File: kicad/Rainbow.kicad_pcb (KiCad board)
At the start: 2 copper layers, 14 parts, among them J1 PICKit3, J2 UART, J3 POWER, J5 RGB, J6 RGB, J7 RGB, J8 RGB, Q1 2N7000, Q2 2N7000, Q3 2N7000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

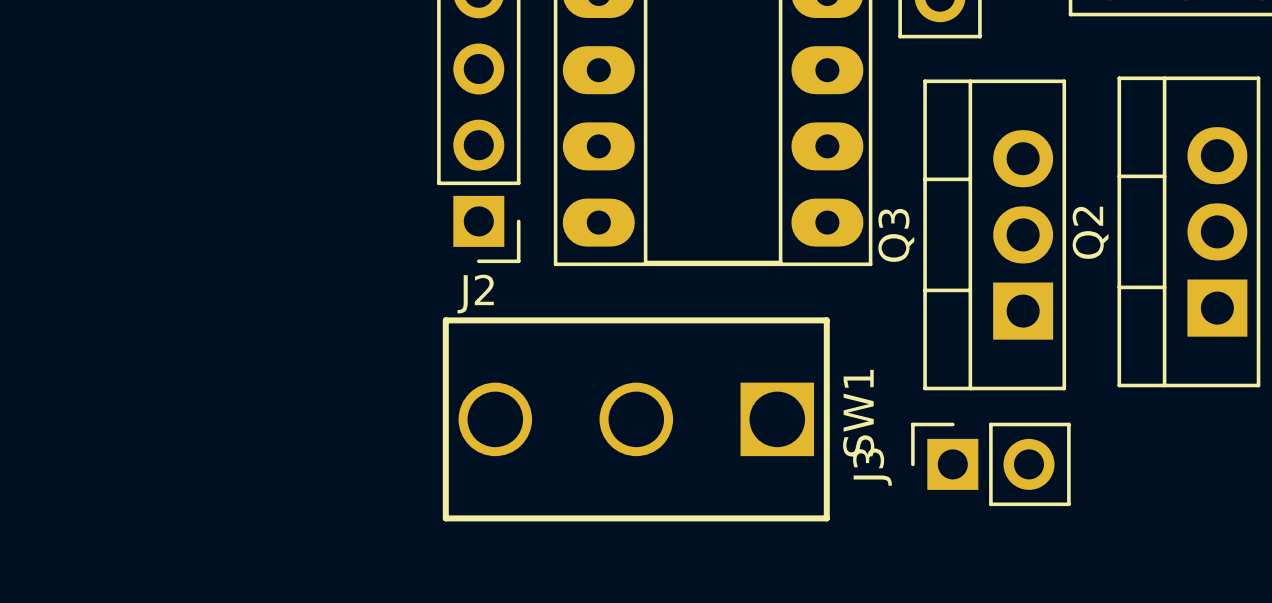
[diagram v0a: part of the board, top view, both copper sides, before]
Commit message: Add capacitors to power supply
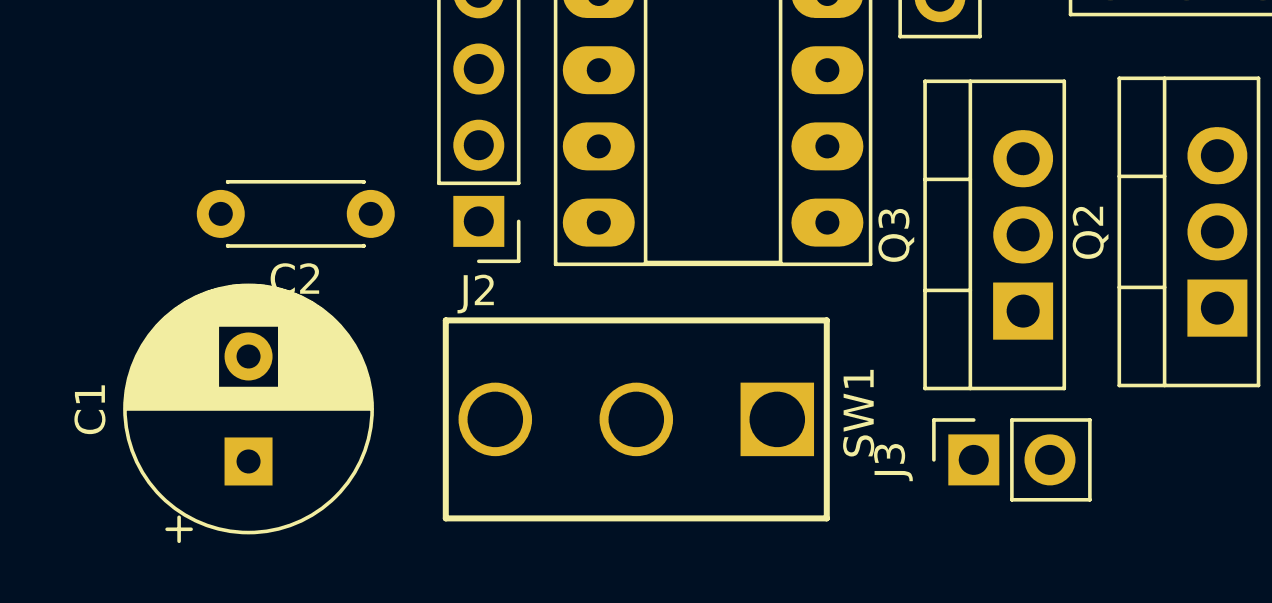
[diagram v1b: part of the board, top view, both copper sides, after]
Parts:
- added C1: 470uF, Capacitor_THT:CP_Radial_D8.0mm_P3.50mm, F.Cu at (107.2, 100.8)
- added C2: 0.1uF, Capacitor_THT:C_Disc_D4.3mm_W1.9mm_P5.00mm, F.Cu at (111.3, 92.5)
- moved J3 0.72 mm to (131.4, 100.7)

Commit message: A bunch of stuff
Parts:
- added J4: JACK, Connector_BarrelJack:BarrelJack_Horizontal, F.Cu at (109.7, 88.4)
- added J9: SOURCE, Connector_PinHeader_2.54mm:PinHeader_1x03_P2.54mm_Vertical, F.Cu at (101.3, 80.9)
- J3: value POWER -> JUMPER
- U1: value PIC16F15323 -> PIC16F15325
- moved J7 52.8 mm to (98.6, 98.3), turned to 0 degrees
- moved J8 47.2 mm to (102.2, 98.3), turned to 0 degrees
- moved J6 41.9 mm to (105.9, 98.3), turned to 0 degrees
- moved J3 40.8 mm to (97.2, 78.5), turned to 0 degrees
- moved J5 36.6 mm to (109.6, 98.2), turned to 0 degrees
- moved C1 31.9 mm to (100.5, 69.6), turned to 180 degrees
- moved SW1 26.5 mm to (107.2, 76.2), turned to 180 degrees
- moved Q1 26.1 mm to (120.5, 92.8), turned to 180 degrees
- moved C2 21.8 mm to (114.7, 71.0), turned to 90 degrees
- moved Q2 19.2 mm to (120.5, 98.5), turned to 180 degrees
- moved R1 15.9 mm to (104.2, 67.9)
- moved Q3 15.1 mm to (120.5, 104.1), turned to 180 degrees
- moved J2 12.0 mm to (125.5, 87.4), turned to 0 degrees
- moved D1 7.54 mm to (119.8, 70.1)
- moved J1 6.18 mm to (125.3, 68.8)
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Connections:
- SW1 pad 1: Net-(J3-Pad1) -> Net-(J9-Pad2)
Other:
- board text added: "LAMBDA"

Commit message: Finish PCB
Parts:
- added H1: MountingHole, MountingHole:MountingHole_2.1mm, F.Cu at (91.8, 95.6)
- added H2: MountingHole, MountingHole:MountingHole_2.1mm, F.Cu at (140.3, 95.7)
- added H3: MountingHole, MountingHole:MountingHole_2.1mm, F.Cu at (91.8, 61.6)
- added H4: MountingHole, MountingHole:MountingHole_2.1mm, F.Cu at (140.3, 61.6)
- J2: value UART -> USB SERIAL
- J4: footprint Connector_BarrelJack:BarrelJack_Horizontal -> Tensility_Barrel_Jack:Tensility_Barrel_Jack
- moved J7 37.2 mm to (131.3, 80.4), turned to 90 degrees
- moved J8 36.1 mm to (131.3, 76.8), turned to 90 degrees
- moved J5 36.1 mm to (131.2, 69.4), turned to 90 degrees
- moved J6 35.7 mm to (131.3, 73.1), turned to 90 degrees
- moved Q3 22.5 mm to (139.3, 91.7), turned to 90 degrees
- moved J4 19.7 mm to (90.1, 86.6)
- moved J2 15.1 mm to (110.6, 89.2), turned to 180 degrees
- moved Q2 14.8 mm to (133.5, 91.7), turned to 90 degrees
- moved SW1 12.7 mm to (96.7, 69.2), turned to -90 degrees
- moved C1 10.6 mm to (110.6, 66.3)
- moved R1 10.4 mm to (114.3, 70.8)
- moved Q1 7.25 mm to (127.6, 91.7), turned to 90 degrees
- moved J9 6.03 mm to (105.9, 77.0), turned to -90 degrees
- moved D1 5.59 mm to (118.1, 64.8), turned to -90 degrees
- moved C2 3.61 mm to (111.2, 72.1), turned to 180 degrees
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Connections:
- J4 pad 3: (no net) -> GNDREF
- U1 pad 10: RED -> BLUE
- U1 pad 8: BLUE -> RED
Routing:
- net Net-(J5-Pad2): track 0.00 -> 20.7 mm
- net MCLR: track 0.00 -> 20.6 mm
- net BLUE: track 0.00 -> 19.6 mm
- net Net-(J5-Pad3): track 0.00 -> 18.4 mm
- net Net-(J5-Pad4): track 0.00 -> 17.4 mm
- net GREEN: track 0.00 -> 14.2 mm
- net LED: track 0.00 -> 8.46 mm
- net RED: track 0.00 -> 5.88 mm
- net Net-(D1-Pad2): track 0.00 -> 5.23 mm
- net ISCPDAT: track 0.00 -> 3.58 mm
- net ISCPCLK: track 0.00 -> 3.58 mm
- net TX: track 0.00 -> 3.55 mm
- net RX: track 0.00 -> 3.55 mm
- added copper zone on F.Cu, net +5V
- added copper zone on B.Cu, net GNDREF
- added copper zone on F.Cu, net GNDREF
- added copper zone on F.Cu, net Net-(J3-Pad1)
- added copper zone on F.Cu, net Net-(J9-Pad1)
- added copper zone on F.Cu, net Net-(J9-Pad2)
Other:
- board outline added: 53.2 x 38.7 mm
- board text added: "5V"
- board text added: "5V/4A MAX"
- board text added: "BLUE"
- board text added: "GND"
- board text added: "GREEN"
- board text added: "OFF"
- board text added: "ON"
- board text added: "PICKit3"
- board text added: "RAINBOW"
- board text added: "RED"
- board text added: "RX"
- board text added: "SOURCE"
- board text added: "TX"
- board text added: "USB SERIAL"
- board text removed: "LAMBDA"

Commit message: Finish up board
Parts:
- moved D1 2.91 mm to (118.3, 67.7), turned to 90 degrees
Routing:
- net Net-(D1-Pad2): track 5.23 -> 8.28 mm
- net MCLR: track 20.6 -> 20.0 mm
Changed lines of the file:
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@@
   )
   (footprint "LED_THT:LED_D5.0mm" (layer "F.Cu")
-    (at 118.1 64.75 -90)
+    (at 118.28 67.65 90)
     (descr "LED, diameter 5.0mm, 2 pins, http://cdn-reichelt.de/documents/datenblatt/A500/LL-504BC2E-009.pdf")
     (tags "LED diameter 5.0mm 2 pins")
@@
     (fp_arc (start -1.23 -1.469694) (mid 4.17 0.000016) (end -1.230016 1.469666) (layer "F.Fab") (width 0.1))
     (fp_circle (center 1.27 0) (end 3.77 0) (layer "F.Fab") (width 0.1) (fill none))
-    (pad "1" thru_hole rect (at 0 0 270) (size 1.8 1.8) (drill 0.9) (layers *.Cu *.Mask)
+    (pad "1" thru_hole rect (at 0 0 90) (size 1.8 1.8) (drill 0.9) (layers *.Cu *.Mask)
       (net 1 "GNDREF") (pinfunction "K") (pintype "passive"))
-    (pad "2" thru_hole circle (at 2.54 0 270) (size 1.8 1.8) (drill 0.9) (layers *.Cu *.Mask)
+    (pad "2" thru_hole circle (at 2.54 0 90) (size 1.8 1.8) (drill 0.9) (layers *.Cu *.Mask)
       (net 2 "Net-(D1-Pad2)") (pinfunction "A") (pintype "passive"))
     (model "${KICAD6_3DMODEL_DIR}/LED_THT.3dshapes/LED_D5.0mm.wrl"
@@
   (gr_line (start 98.8 94.37) (end 100.81 94.38) (layer "F.SilkS") (width 0.15))
   (gr_line (start 103.325 81.7) (end 103.325 80.525) (layer "F.SilkS") (width 0.15))
-  (gr_arc (start 100.110069 93.978157) (mid 101.009971 93.580113) (end 101.615253 94.355934) (layer "F.SilkS") (width 0.15))
+  (gr_arc (start 100.110069 93.978157) (mid 101.009971 93.580114) (end 101.615253 94.355934) (layer "F.SilkS") (width 0.15))
   (gr_poly
     (pts
@@
     (effects (font (size 1.2 1.2) (thickness 0.2)))
   )
-  (segment (start 121.885 70.775) (end 118.4 67.29) (width 0.5) (layer "B.Cu") (net 2))
-  (segment (start 118.4 67.29) (end 118.1 67.29) (width 0.5) (layer "B.Cu") (net 2))
+  (segment (start 120.2 65.11) (end 118.28 65.11) (width 0.5) (layer "B.Cu") (net 2))
+  (segment (start 121.885 70.775) (end 121.885 66.795) (width 0.5) (layer "B.Cu") (net 2))
+  (segment (start 121.885 66.795) (end 120.2 65.11) (width 0.5) (layer "B.Cu") (net 2))
   (segment (start 120.4 68.825) (end 118.025 71.2) (width 0.5) (layer "F.Cu") (net 3))
-  (segment (start 114.805 81.52) (end 114.15 81.52) (width 0.5) (layer "F.Cu") (net 3))
   (segment (start 118.025 78.3) (end 114.805 81.52) (width 0.5) (layer "F.Cu") (net 3))
   (segment (start 118.025 71.2) (end 118.025 78.3) (width 0.5) (layer "F.Cu") (net 3))
   (segment (start 125.35 68.825) (end 120.4 68.825) (width 0.5) (layer "F.Cu") (net 3))
   (segment (start 125.35 76.445) (end 121.775 76.445) (width 0.5) (layer "F.Cu") (net 5))
-  (segment (start 121.775 76.445) (end 121.77 76.44) (width 0.5) (layer "F.Cu") (net 5))
   (segment (start 125.35 78.985) (end 121.775 78.985) (width 0.5) (layer "F.Cu") (net 6))
-  (segment (start 121.775 78.985) (end 121.77 78.98) (width 0.5) (layer "F.Cu") (net 6))
   (segment (start 114.15 86.6) (end 110.61 86.6) (width 0.5) (layer "F.Cu") (net 9))
-  (segment (start 110.61 86.6) (end 110.6 86.61) (width 0.5) (layer "F.Cu") (net 9))
   (segment (start 114.15 84.06) (end 110.61 84.06) (width 0.5) (layer "F.Cu") (net 10))
-  (segment (start 110.61 84.06) (end 110.6 84.07) (width 0.5) (layer "F.Cu") (net 10))
   (segment (start 133.815 76.75) (end 133.815 73.075) (width 2) (layer "B.Cu") (net 14))
   (segment (start 133.815 81.959022) (end 129.189022 86.585) (width 2) (layer "B.Cu") (net 14))
@@
   (segment (start 138.87 73.05) (end 138.895 73.075) (width 2) (layer "B.Cu") (net 16))
   (segment (start 121.77 89.14) (end 127.63 89.14) (width 0.5) (layer "F.Cu") (net 17))
-  (segment (start 127.63 89.14) (end 127.645 89.125) (width 0.5) (layer "F.Cu") (net 17))
   (segment (start 124.525 86.6) (end 121.77 86.6) (width 0.5) (layer "F.Cu") (net 18))
   (segment (start 133.545 89.12) (end 129.4 84.975) (width 0.5) (layer "F.Cu") (net 18))
   (segment (start 126.15 84.975) (end 124.525 86.6) (width 0.5) (layer "F.Cu") (net 18))
-  (segment (start 133.545 89.125) (end 133.545 89.12) (width 0.5) (layer "F.Cu") (net 18))
   (segment (start 129.4 84.975) (end 126.15 84.975) (width 0.5) (layer "F.Cu") (net 18))
   (segment (start 121.77 84.06) (end 134.21 84.06) (width 0.5) (layer "F.Cu") (net 19))
   (segment (start 134.21 84.06) (end 139.27 89.12) (width 0.5) (layer "F.Cu") (net 19))
-  (segment (start 139.27 89.12) (end 139.27 89.125) (width 0.5) (layer "F.Cu") (net 19))
   (segment (start 116.475 72.375) (end 116.475 75.075) (width 0.5) (layer "F.Cu") (net 20))
   (segment (start 116.475 75.075) (end 115.11 76.44) (width 0.5) (layer "F.Cu") (net 20))
